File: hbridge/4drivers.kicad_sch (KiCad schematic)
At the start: 1 part, among them U14 driver_MOSFET_board

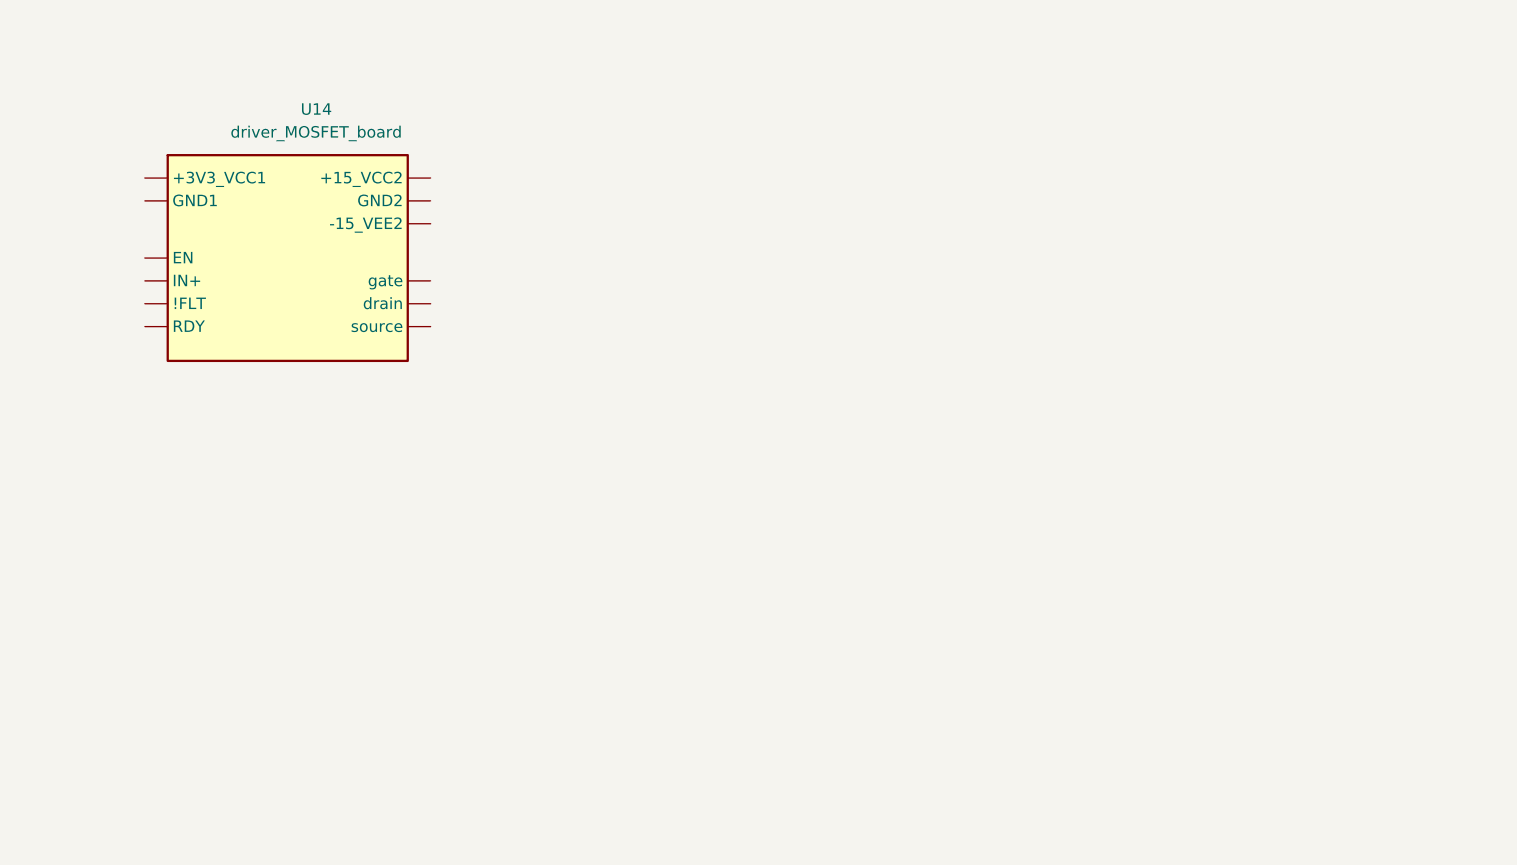
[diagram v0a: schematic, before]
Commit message: Half-bridge refactoring start.
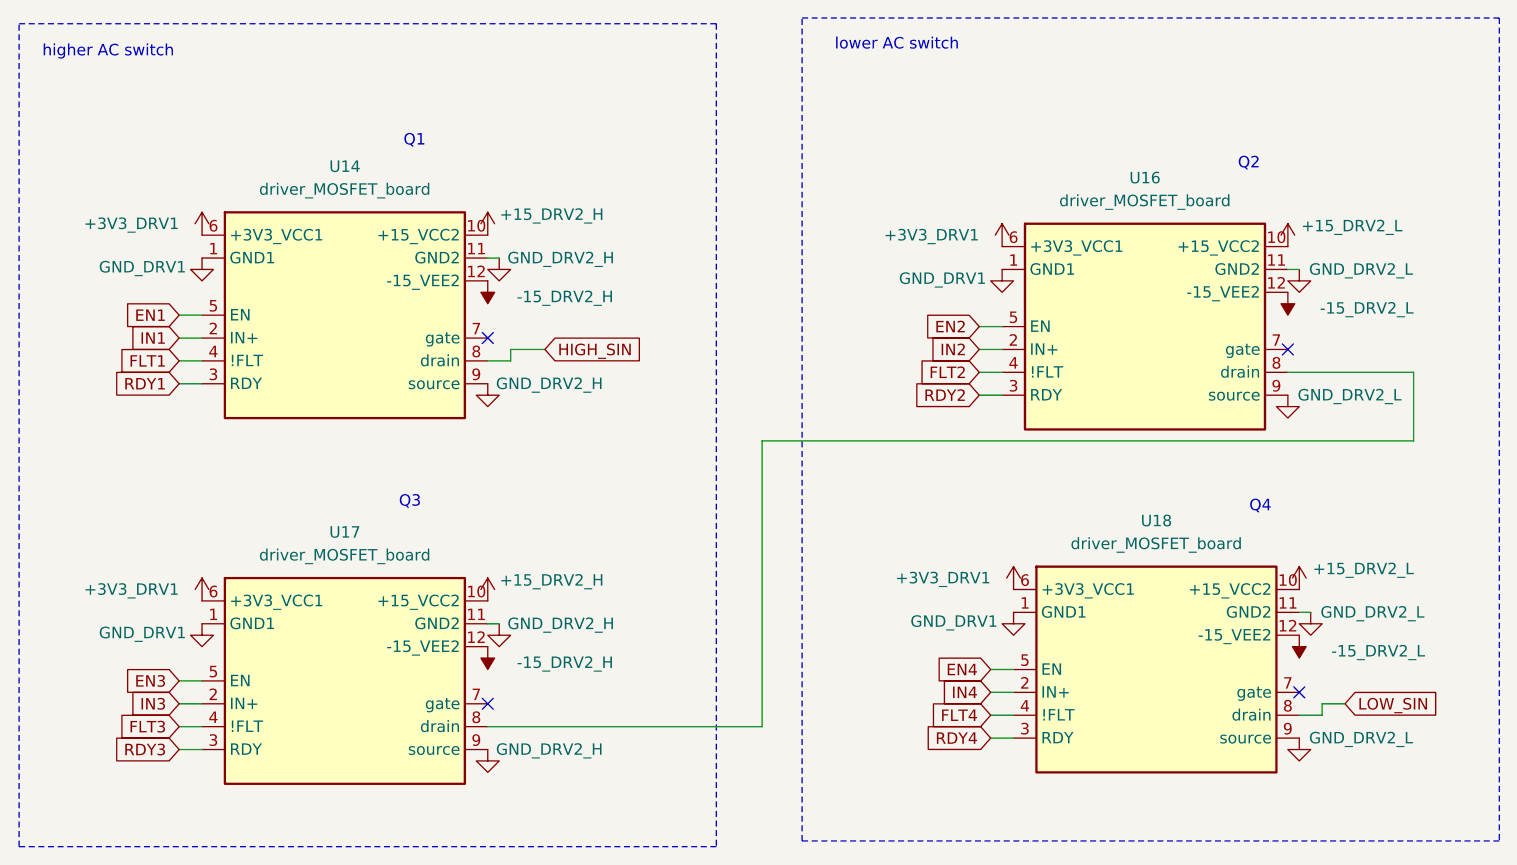
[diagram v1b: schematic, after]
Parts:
- added U16, U17, U18: driver_MOSFET_board, Tamara:плата драйвера, symbol Tamara:driver_MOSFET_board
- U14: footprint Package_SO:SOIC-8_3.9x4.9mm_P1.27mm -> Tamara:плата драйвера
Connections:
- new net: U16.8 (drain), U17.8 (drain)
- new net +15_DRV2_H: U14.10 (+15_VCC2), U17.10 (+15_VCC2)
- new net +15_DRV2_L: U16.10 (+15_VCC2), U18.10 (+15_VCC2)
- new net +3V3_DRV1: U14.6 (+3V3_VCC1), U16.6 (+3V3_VCC1), U17.6 (+3V3_VCC1), U18.6 (+3V3_VCC1)
- new net -15_DRV2_H: U14.12 (-15_VEE2), U17.12 (-15_VEE2)
- new net -15_DRV2_L: U16.12 (-15_VEE2), U18.12 (-15_VEE2)
- new net EN1: U14.5 (EN)
- new net EN2: U16.5 (EN)
- new net EN3: U17.5 (EN)
- new net EN4: U18.5 (EN)
- new net FLT1: U14.4 (!FLT)
- new net FLT2: U16.4 (!FLT)
- new net FLT3: U17.4 (!FLT)
- new net FLT4: U18.4 (!FLT)
- new net GND_DRV1: U14.1 (GND1), U16.1 (GND1), U17.1 (GND1), U18.1 (GND1)
- new net GND_DRV2_H: U14.11 (GND2), U14.9 (source), U17.11 (GND2), U17.9 (source)
- new net GND_DRV2_L: U16.11 (GND2), U16.9 (source), U18.11 (GND2), U18.9 (source)
- new net HIGH_SIN: U14.8 (drain)
- new net IN1: U14.2 (IN+)
- new net IN2: U16.2 (IN+)
- new net IN3: U17.2 (IN+)
- new net IN4: U18.2 (IN+)
- new net LOW_SIN: U18.8 (drain)
- new net RDY1: U14.3 (RDY)
- new net RDY2: U16.3 (RDY)
- new net RDY3: U17.3 (RDY)
- new net RDY4: U18.3 (RDY)
- no-connect marks 0 -> 4
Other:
- note added: "Q1"
- note added: "Q2"
- note added: "Q3"
- note added: "Q4"
- note added: "higher AC switch"
- note added: "lower AC switch"
